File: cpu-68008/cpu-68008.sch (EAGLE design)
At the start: 54 parts, among them IC1 68008, IC11 NE555, IC2 AS6C4008, IC3 39SF010, IC4 DS1244Y, IC5 XR68C681, Q1 8MHz, Q2 3.6864MHz

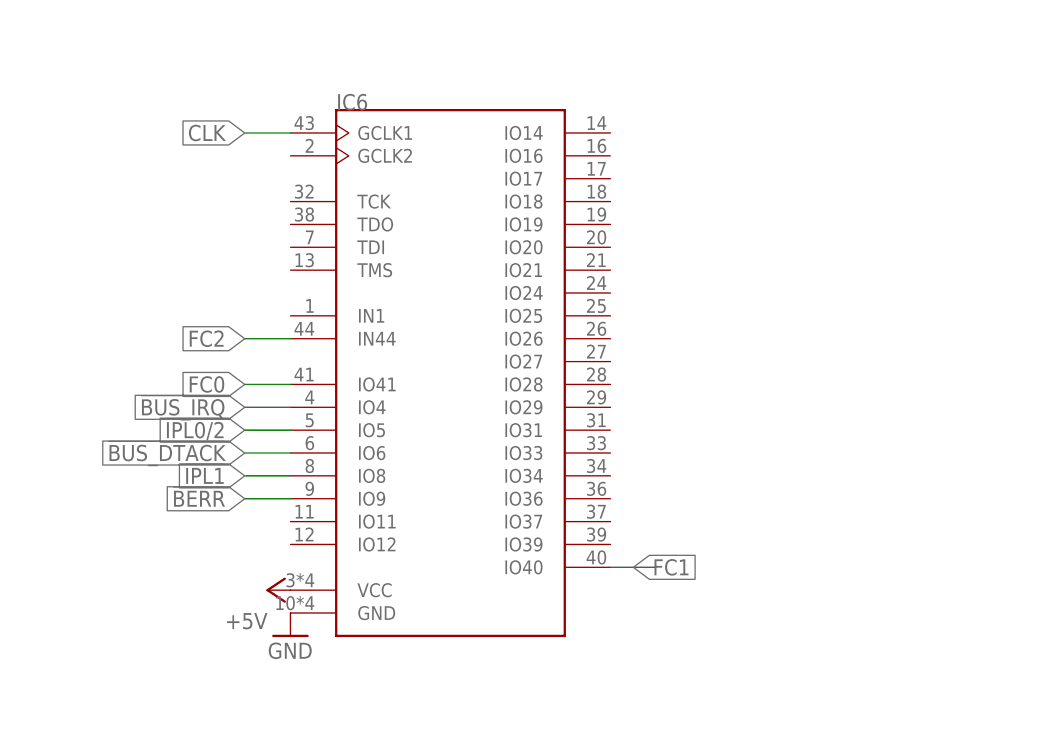
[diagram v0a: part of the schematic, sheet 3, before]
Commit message: more stuff got routed for 68008
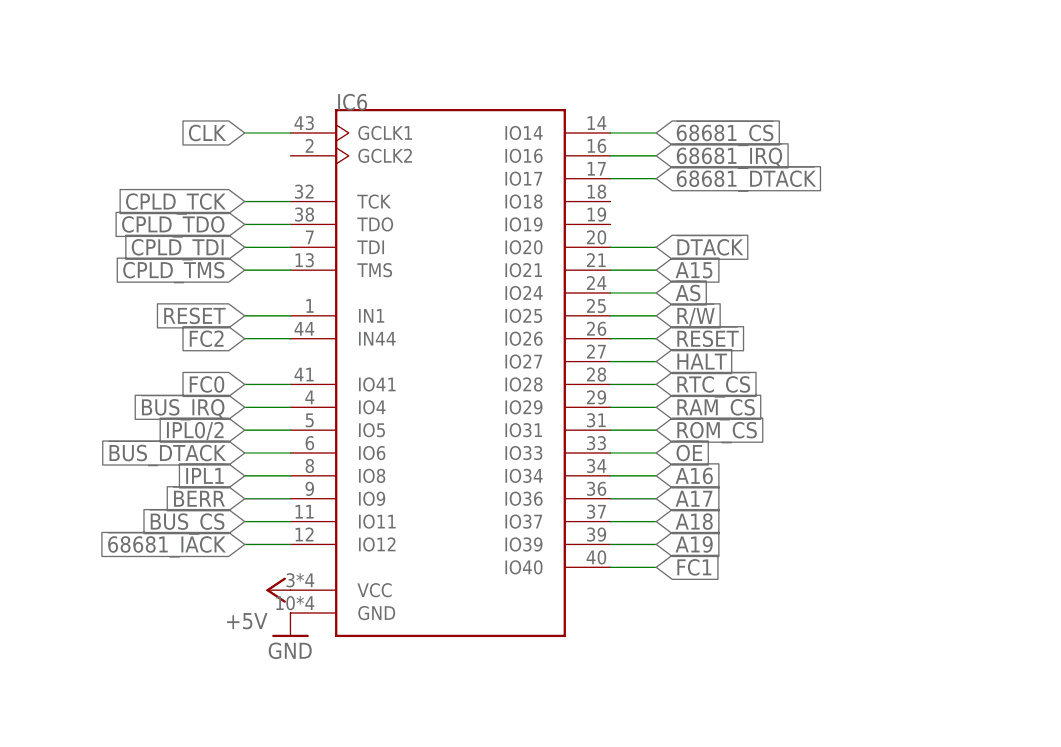
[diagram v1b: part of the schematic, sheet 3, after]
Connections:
- removed net 68681_IRQ: IC5.!INTR
- new net !68681_IRQ: IC5.!INTR, IC6.IO16
- new net !BUS_CS: IC6.IO11, SV6.7
- net !68681_CS: now also IC6.IO14
- net !68681_DTACK: now also IC6.IO17
- net !68681_IACK: now also IC6.IO12
- net !AS: now also IC6.IO24
- net !DTACK: now also IC6.IO20
- net !HALT: now also IC6.IO27
- net !OE: now also IC6.IO33
- net !RAM_CS: now also IC6.IO29
- net !RESET: now also IC6.IO26
- net !ROM_CS: now also IC6.IO31
- net !RTC_CS: now also IC6.IO28
- net A15: now also IC6.IO21
- net A16: now also IC6.IO34
- net A17: now also IC6.IO36
- net A18: now also IC6.IO37
- net A19: now also IC6.IO39
- net CPLD_TCK: now also IC6.TCK
- net CPLD_TDI: now also IC6.TDI
- net CPLD_TDO: now also IC6.TDO
- net CPLD_TMS: now also IC6.TMS
- net R/!W!: now also IC6.IO25
- net RESET: now also IC6.IN1
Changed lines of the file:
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@@
 </instances>
 <busses>
-<bus name="68681_CLK,!68681_CS,!68681_DTACK,!68681_IACK,68681_IRQ,A[0..19],D[0..7],IO_IN[0..5],IO_OUT[0..5],!IPL1,!OE,OUT[0..1],!RESET,!RTC_CS,R/!W!,STATUS[0..1],UART0_RX,UART0_TX,UART1_RX,UART1_TX">
+<bus name="68681_CLK,!68681_CS,!68681_DTACK,!68681_IACK,!68681_IRQ,A[0..19],D[0..7],IO_IN[0..5],IO_OUT[0..5],!IPL1,!OE,OUT[0..1],!RESET,!RTC_CS,R/!W!,STATUS[0..1],UART0_RX,UART0_TX,UART1_RX,UART1_TX">
 <segment>
 <wire x1="25.4" y1="177.8" x2="68.58" y2="177.8" width="0.762" layer="92"/>
@@
 </segment>
 </bus>
-<bus name="A[0..19],!AS,!BERR,!BG,!BR,!BUS_DTACK,!BUS_IRQ,CLK,D[0..7],!DS,!DTACK,E,FC[0..2],!HALT,!RESET,R/!W!,!VPA">
+<bus name="A[0..19],!AS,!BERR,!BG,!BR,!BUS_CS,!BUS_DTACK,!BUS_IRQ,CLK,D[0..7],!DS,!DTACK,E,FC[0..2],!HALT,!RESET,R/!W!,!VPA">
 <segment>
 <wire x1="71.12" y1="33.02" x2="71.12" y2="2.54" width="0.762" layer="92"/>
@@
 </segment>
 </net>
-<net name="68681_IRQ" class="0">
+<net name="!68681_IRQ" class="0">
 <segment>
 <pinref part="IC5" gate="G$1" pin="!INTR"/>
@@
 <wire x1="78.74" y1="12.7" x2="73.66" y2="12.7" width="0.1524" layer="91"/>
 <wire x1="73.66" y1="12.7" x2="71.12" y2="10.16" width="0.1524" layer="91"/>
+</segment>
+</net>
+<net name="!BUS_CS" class="0">
+<segment>
+<pinref part="SV6" gate="1" pin="7"/>
+<wire x1="93.98" y1="15.24" x2="99.06" y2="15.24" width="0.1524" layer="91"/>
+<wire x1="99.06" y1="15.24" x2="101.6" y2="12.7" width="0.1524" layer="91"/>
 </segment>
 </net>
@@
 <label x="236.22" y="63.5" size="1.778" layer="95" xref="yes"/>
 </segment>
+<segment>
+<pinref part="IC6" gate="G$1" pin="IN1"/>
+<wire x1="48.26" y1="152.4" x2="43.18" y2="152.4" width="0.1524" layer="91"/>
+<label x="43.18" y="152.4" size="1.778" layer="95" rot="R180" xref="yes"/>
+</segment>
 </net>
 <net name="N$1" class="0">
@@
 <label x="172.72" y="137.16" size="1.778" layer="95" xref="yes"/>
 </segment>
+<segment>
+<pinref part="IC6" gate="G$1" pin="TMS"/>
+<wire x1="48.26" y1="157.48" x2="43.18" y2="157.48" width="0.1524" layer="91"/>
+<label x="43.18" y="157.48" size="1.778" layer="95" rot="R180" xref="yes"/>
+</segment>
 </net>
 <net name="CPLD_TDI" class="0">
@@
 <label x="172.72" y="139.7" size="1.778" layer="95" xref="yes"/>
 </segment>
+<segment>
+<pinref part="IC6" gate="G$1" pin="TDI"/>
+<wire x1="48.26" y1="160.02" x2="43.18" y2="160.02" width="0.1524" layer="91"/>
+<label x="43.18" y="160.02" size="1.778" layer="95" rot="R180" xref="yes"/>
+</segment>
 </net>
 <net name="CPLD_TDO" class="0">
@@
 <label x="172.72" y="142.24" size="1.778" layer="95" xref="yes"/>
 </segment>
+<segment>
+<pinref part="IC6" gate="G$1" pin="TDO"/>
+<wire x1="48.26" y1="162.56" x2="43.18" y2="162.56" width="0.1524" layer="91"/>
+<label x="43.18" y="162.56" size="1.778" layer="95" rot="R180" xref="yes"/>
+</segment>
 </net>
 <net name="CPLD_TCK" class="0">
@@
 <label x="172.72" y="144.78" size="1.778" layer="95" xref="yes"/>
 </segment>
+<segment>
+<pinref part="IC6" gate="G$1" pin="TCK"/>
+<wire x1="48.26" y1="165.1" x2="43.18" y2="165.1" width="0.1524" layer="91"/>
+<label x="43.18" y="165.1" size="1.778" layer="95" rot="R180" xref="yes"/>
+</segment>
 </net>
 <net name="!BUS_DTACK" class="0">
@@
 <pinref part="IC6" gate="G$1" pin="IO40"/>
 <wire x1="83.82" y1="124.46" x2="88.9" y2="124.46" width="0.1524" layer="91"/>
-<label x="86.36" y="124.46" size="1.778" layer="95" xref="yes"/>
+<label x="88.9" y="124.46" size="1.778" layer="95" xref="yes"/>
 </segment>
 </net>
@@
 </segment>
 </net>
+<net name="!BUS_CS" class="0">
+<segment>
+<pinref part="IC6" gate="G$1" pin="IO11"/>
+<wire x1="48.26" y1="129.54" x2="43.18" y2="129.54" width="0.1524" layer="91"/>
+<label x="43.18" y="129.54" size="1.778" layer="95" rot="R180" xref="yes"/>
+</segment>
+</net>
+<net name="!RTC_CS" class="0">
+<segment>
+<pinref part="IC6" gate="G$1" pin="IO28"/>
+<wire x1="83.82" y1="144.78" x2="88.9" y2="144.78" width="0.1524" layer="91"/>
+<label x="88.9" y="144.78" size="1.778" layer="95" xref="yes"/>
+</segment>
+</net>
+<net name="!RAM_CS" class="0">
+<segment>
+<pinref part="IC6" gate="G$1" pin="IO29"/>
+<wire x1="83.82" y1="142.24" x2="88.9" y2="142.24" width="0.1524" layer="91"/>
+<label x="88.9" y="142.24" size="1.778" layer="95" xref="yes"/>
+</segment>
+</net>
+<net name="!ROM_CS" class="0">
+<segment>
+<pinref part="IC6" gate="G$1" pin="IO31"/>
+<wire x1="83.82" y1="139.7" x2="88.9" y2="139.7" width="0.1524" layer="91"/>
+<label x="88.9" y="139.7" size="1.778" layer="95" xref="yes"/>
+</segment>
+</net>
+<net name="!68681_DTACK" class="0">
+<segment>
+<pinref part="IC6" gate="G$1" pin="IO17"/>
+<wire x1="83.82" y1="167.64" x2="88.9" y2="167.64" width="0.1524" layer="91"/>
+<label x="88.9" y="167.64" size="1.778" layer="95" xref="yes"/>
+</segment>
+</net>
+<net name="!OE" class="0">
+<segment>
+<pinref part="IC6" gate="G$1" pin="IO33"/>
+<wire x1="83.82" y1="137.16" x2="88.9" y2="137.16" width="0.1524" layer="91"/>
+<label x="88.9" y="137.16" size="1.778" layer="95" xref="yes"/>
+</segment>
+</net>
+<net name="A19" class="0">
+<segment>
+<pinref part="IC6" gate="G$1" pin="IO39"/>
+<wire x1="83.82" y1="127" x2="88.9" y2="127" width="0.1524" layer="91"/>
+<label x="88.9" y="127" size="1.778" layer="95" xref="yes"/>
+</segment>
+</net>
+<net name="A18" class="0">
+<segment>
+<pinref part="IC6" gate="G$1" pin="IO37"/>
+<wire x1="83.82" y1="129.54" x2="88.9" y2="129.54" width="0.1524" layer="91"/>
+<label x="88.9" y="129.54" size="1.778" layer="95" xref="yes"/>
+</segment>
+</net>
+<net name="A17" class="0">
+<segment>
+<pinref part="IC6" gate="G$1" pin="IO36"/>
+<wire x1="83.82" y1="132.08" x2="88.9" y2="132.08" width="0.1524" layer="91"/>
+<label x="88.9" y="132.08" size="1.778" layer="95" xref="yes"/>
+</segment>
+</net>
+<net name="A16" class="0">
+<segment>
+<pinref part="IC6" gate="G$1" pin="IO34"/>
+<wire x1="83.82" y1="134.62" x2="88.9" y2="134.62" width="0.1524" layer="91"/>
+<label x="88.9" y="134.62" size="1.778" layer="95" xref="yes"/>
+</segment>
+</net>
+<net name="!HALT" class="0">
+<segment>
+<pinref part="IC6" gate="G$1" pin="IO27"/>
+<wire x1="83.82" y1="147.32" x2="88.9" y2="147.32" width="0.1524" layer="91"/>
+<label x="88.9" y="147.32" size="1.778" layer="95" xref="yes"/>
+</segment>
+</net>
+<net name="!DTACK" class="0">
+<segment>
+<pinref part="IC6" gate="G$1" pin="IO20"/>
+<wire x1="83.82" y1="160.02" x2="88.9" y2="160.02" width="0.1524" layer="91"/>
+<label x="88.9" y="160.02" size="1.778" layer="95" xref="yes"/>
+</segment>
+</net>
+<net name="A15" class="0">
+<segment>
+<pinref part="IC6" gate="G$1" pin="IO21"/>
+<wire x1="83.82" y1="157.48" x2="88.9" y2="157.48" width="0.1524" layer="91"/>
+<label x="88.9" y="157.48" size="1.778" layer="95" xref="yes"/>
+</segment>
+</net>
+<net name="!AS" class="0">
+<segment>
+<pinref part="IC6" gate="G$1" pin="IO24"/>
+<wire x1="83.82" y1="154.94" x2="88.9" y2="154.94" width="0.1524" layer="91"/>
+<label x="88.9" y="154.94" size="1.778" layer="95" xref="yes"/>
+</segment>
+</net>
+<net name="R/!W!" class="0">
+<segment>
+<pinref part="IC6" gate="G$1" pin="IO25"/>
+<wire x1="83.82" y1="152.4" x2="88.9" y2="152.4" width="0.1524" layer="91"/>
+<label x="88.9" y="152.4" size="1.778" layer="95" xref="yes"/>
+</segment>
+</net>
+<net name="!RESET" class="0">
+<segment>
+<pinref part="IC6" gate="G$1" pin="IO26"/>
+<wire x1="83.82" y1="149.86" x2="88.9" y2="149.86" width="0.1524" layer="91"/>
+<label x="88.9" y="149.86" size="1.778" layer="95" xref="yes"/>
+</segment>
+</net>
+<net name="!68681_CS" class="0">
+<segment>
+<pinref part="IC6" gate="G$1" pin="IO14"/>
+<wire x1="83.82" y1="172.72" x2="88.9" y2="172.72" width="0.1524" layer="91"/>
+<label x="88.9" y="172.72" size="1.778" layer="95" xref="yes"/>
+</segment>
+</net>
+<net name="!68681_IACK" class="0">
+<segment>
+<pinref part="IC6" gate="G$1" pin="IO12"/>
+<wire x1="48.26" y1="127" x2="43.18" y2="127" width="0.1524" layer="91"/>
+<label x="43.18" y="127" size="1.778" layer="95" rot="R180" xref="yes"/>
+</segment>
+</net>
+<net name="!68681_IRQ" class="0">
+<segment>
+<pinref part="IC6" gate="G$1" pin="IO16"/>
+<wire x1="83.82" y1="170.18" x2="88.9" y2="170.18" width="0.1524" layer="91"/>
+<label x="88.9" y="170.18" size="1.778" layer="95" xref="yes"/>
+</segment>
+</net>

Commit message: finished routing CPLD
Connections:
- net !AS: now also IC6.IO27; no longer IC6.IO24
- net !DTACK: now also IC6.IO36; no longer IC6.IO20
- net !HALT: now also IC6.IO37; no longer IC6.IO27
- net !RESET: now also IC6.IO39; no longer IC6.IO26
- net A15: now also IC6.IO26; no longer IC6.IO21
- net A16: now also IC6.IO25; no longer IC6.IO34
- net A17: now also IC6.IO24; no longer IC6.IO36
- net A18: now also IC6.IO21; no longer IC6.IO37
- net A19: now also IC6.IO20; no longer IC6.IO39
- net R/!W!: now also IC6.IO34; no longer IC6.IO25
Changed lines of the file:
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@@
 </segment>
 </net>
-<net name="A19" class="0">
+<net name="A17" class="0">
 <segment>
-<pinref part="IC6" gate="G$1" pin="IO39"/>
-<wire x1="83.82" y1="127" x2="88.9" y2="127" width="0.1524" layer="91"/>
-<label x="88.9" y="127" size="1.778" layer="95" xref="yes"/>
+<pinref part="IC6" gate="G$1" pin="IO24"/>
+<wire x1="83.82" y1="154.94" x2="88.9" y2="154.94" width="0.1524" layer="91"/>
+<label x="88.9" y="154.94" size="1.778" layer="95" xref="yes"/>
 </segment>
 </net>
-<net name="A18" class="0">
+<net name="!HALT" class="0">
 <segment>
 <pinref part="IC6" gate="G$1" pin="IO37"/>
@@
 </segment>
 </net>
-<net name="A17" class="0">
+<net name="A15" class="0">
 <segment>
-<pinref part="IC6" gate="G$1" pin="IO36"/>
-<wire x1="83.82" y1="132.08" x2="88.9" y2="132.08" width="0.1524" layer="91"/>
-<label x="88.9" y="132.08" size="1.778" layer="95" xref="yes"/>
+<pinref part="IC6" gate="G$1" pin="IO26"/>
+<wire x1="83.82" y1="149.86" x2="88.9" y2="149.86" width="0.1524" layer="91"/>
+<label x="88.9" y="149.86" size="1.778" layer="95" xref="yes"/>
 </segment>
 </net>
-<net name="A16" class="0">
-<segment>
-<pinref part="IC6" gate="G$1" pin="IO34"/>
-<wire x1="83.82" y1="134.62" x2="88.9" y2="134.62" width="0.1524" layer="91"/>
-<label x="88.9" y="134.62" size="1.778" layer="95" xref="yes"/>
-</segment>
-</net>
-<net name="!HALT" class="0">
+<net name="!AS" class="0">
 <segment>
 <pinref part="IC6" gate="G$1" pin="IO27"/>
@@
 </segment>
 </net>
-<net name="!DTACK" class="0">
-<segment>
-<pinref part="IC6" gate="G$1" pin="IO20"/>
-<wire x1="83.82" y1="160.02" x2="88.9" y2="160.02" width="0.1524" layer="91"/>
-<label x="88.9" y="160.02" size="1.778" layer="95" xref="yes"/>
-</segment>
-</net>
-<net name="A15" class="0">
-<segment>
-<pinref part="IC6" gate="G$1" pin="IO21"/>
-<wire x1="83.82" y1="157.48" x2="88.9" y2="157.48" width="0.1524" layer="91"/>
-<label x="88.9" y="157.48" size="1.778" layer="95" xref="yes"/>
-</segment>
-</net>
-<net name="!AS" class="0">
-<segment>
-<pinref part="IC6" gate="G$1" pin="IO24"/>
-<wire x1="83.82" y1="154.94" x2="88.9" y2="154.94" width="0.1524" layer="91"/>
-<label x="88.9" y="154.94" size="1.778" layer="95" xref="yes"/>
-</segment>
-</net>
 <net name="R/!W!" class="0">
 <segment>
-<pinref part="IC6" gate="G$1" pin="IO25"/>
-<wire x1="83.82" y1="152.4" x2="88.9" y2="152.4" width="0.1524" layer="91"/>
-<label x="88.9" y="152.4" size="1.778" layer="95" xref="yes"/>
-</segment>
-</net>
-<net name="!RESET" class="0">
-<segment>
-<pinref part="IC6" gate="G$1" pin="IO26"/>
-<wire x1="83.82" y1="149.86" x2="88.9" y2="149.86" width="0.1524" layer="91"/>
-<label x="88.9" y="149.86" size="1.778" layer="95" xref="yes"/>
+<pinref part="IC6" gate="G$1" pin="IO34"/>
+<wire x1="83.82" y1="134.62" x2="88.9" y2="134.62" width="0.1524" layer="91"/>
+<label x="88.9" y="134.62" size="1.778" layer="95" xref="yes"/>
 </segment>
 </net>
@@
 </segment>
 </net>
+<net name="!RESET" class="0">
+<segment>
+<pinref part="IC6" gate="G$1" pin="IO39"/>
+<wire x1="83.82" y1="127" x2="88.9" y2="127" width="0.1524" layer="91"/>
+<label x="88.9" y="127" size="1.778" layer="95" xref="yes"/>
+</segment>
+</net>
+<net name="!DTACK" class="0">
+<segment>
+<pinref part="IC6" gate="G$1" pin="IO36"/>
+<wire x1="83.82" y1="132.08" x2="88.9" y2="132.08" width="0.1524" layer="91"/>
+<label x="88.9" y="132.08" size="1.778" layer="95" xref="yes"/>
+</segment>
+</net>
+<net name="A16" class="0">
+<segment>
+<pinref part="IC6" gate="G$1" pin="IO25"/>
+<wire x1="83.82" y1="152.4" x2="88.9" y2="152.4" width="0.1524" layer="91"/>
+<label x="88.9" y="152.4" size="1.778" layer="95" xref="yes"/>
+</segment>
+</net>
+<net name="A18" class="0">
+<segment>
+<pinref part="IC6" gate="G$1" pin="IO21"/>
+<wire x1="83.82" y1="157.48" x2="88.9" y2="157.48" width="0.1524" layer="91"/>
+<label x="88.9" y="157.48" size="1.778" layer="95" xref="yes"/>
+</segment>
+</net>
+<net name="A19" class="0">
+<segment>
+<pinref part="IC6" gate="G$1" pin="IO20"/>
+<wire x1="83.82" y1="160.02" x2="88.9" y2="160.02" width="0.1524" layer="91"/>
+<label x="88.9" y="160.02" size="1.778" layer="95" xref="yes"/>
+</segment>
+</net>

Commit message: routed duart IO and serial channels
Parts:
- added Q3: (no value), crystal:CRYSTALHC49S
- added R19, R2, R20, R3: 10k, rcl:R-EU_R2012
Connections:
- net !68681_IRQ: now also R20.1
- net !BG: now also R3.2
- net !BR: now also R2.2
- net !VPA: now also IC6.IO18, R19.2
- net +5V: now also R19.1, R2.1, R20.2
- net GND: now also R3.1, SV6.10, SV6.11, SV6.12, SV6.8, SV6.9
- net IO_IN0: now also IC5.IP2; no longer IC5.IP0
- net IO_IN1: now also IC5.IP5; no longer IC5.IP1
- net IO_IN2: now also IC5.IP4; no longer IC5.IP2
- net IO_IN4: now also IC5.IP1; no longer IC5.IP4
- net IO_IN5: now also IC5.IP0; no longer IC5.IP5
- net IO_OUT0: now also IC5.OP2; no longer IC5.OP0
- net IO_OUT1: now also IC5.OP0; no longer IC5.OP1
- net IO_OUT2: now also IC5.OP6; no longer IC5.OP2
- net IO_OUT3: now also IC5.OP4; no longer IC5.OP3
- net IO_OUT4: now also IC5.OP1; no longer IC5.OP4
- net STATUS0: now also IC5.OP3; no longer IC5.OP6
- net UART0_RX: now also SV5.2; no longer SV5.4
- net UART0_TX: now also SV5.1; no longer SV5.3
- net UART1_RX: now also SV5.4; no longer SV5.2
- net UART1_TX: now also SV5.3; no longer SV5.1

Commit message: cleaned up routing for duart, added new duart clock circuit
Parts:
- removed Q2: 3.6864MHz, crystal:XO-8
- added C13: 27pF, rcl:C-EUC0805
- added C15, C16, C22: 100nF, rcl:C-EUC0805
- added C17: 10µF, rcl:CPOL-EUSMCB
- added R21, R22: 100R, rcl:R-EU_R2012
- C7: value 100nF -> 27pF; MOUSER 710-885012207072 -> 80-C0805C270K5HACTU
- Q3: value (none) -> 3.6864 MHz; MOUSER (none) -> 669-E1UFA18-3.6864M
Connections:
- removed net 68681_CLK: IC5.X1/CLK, Q2.OUT
- new net 68681_X1: IC5.X1/CLK, R22.2
- new net 68681_X2: IC5.X2, R21.2
- new net N$2: C7.2, Q3.1, R22.1
- new net N$3: C13.2, Q3.2, R21.1
- net +5V: now also C15.1, C16.1, C17.+, C22.1; no longer C7.1, Q2.VCC
- net GND: now also C13.1, C15.2, C16.2, C17.-, C22.2, C7.1; no longer C7.2, Q2.GND
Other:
- note added: "C20 for IC11 C9, C12, C14 for IC6"
- note removed: "C20 for IC11 C9, C12 for IC6"
- moved on the sheet: C12, C4, C7, C9, Q3
